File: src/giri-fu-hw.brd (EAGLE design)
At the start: 91.1 x 54.6 mm, 30 parts, among them IC1 ATMEGA168-20P, IC2 7805T, IC3 ULN2003AN, K1 G5V1, K2 G5V1, K3 G5V1, K4 G5V1, K5 G5V1, K6 G5V1, Q1 16MHz

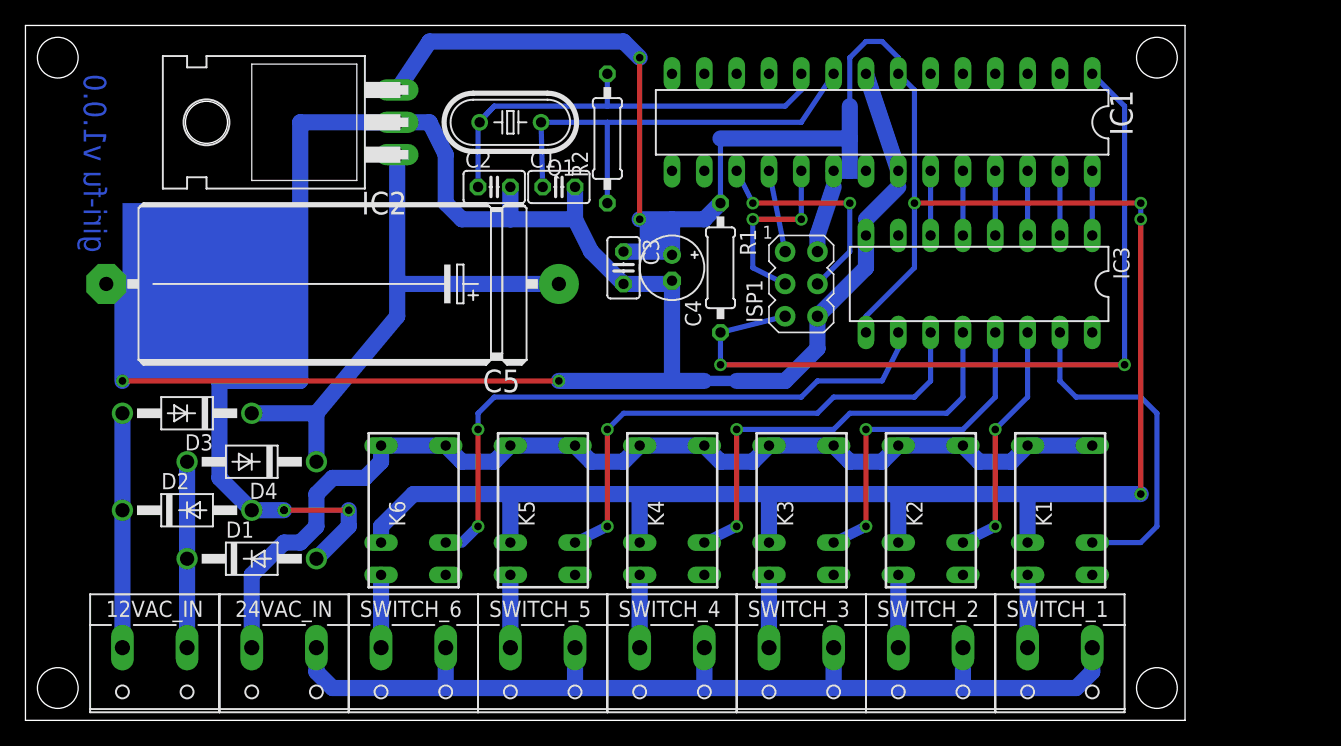
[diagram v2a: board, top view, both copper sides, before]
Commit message: Add RS485 adapter
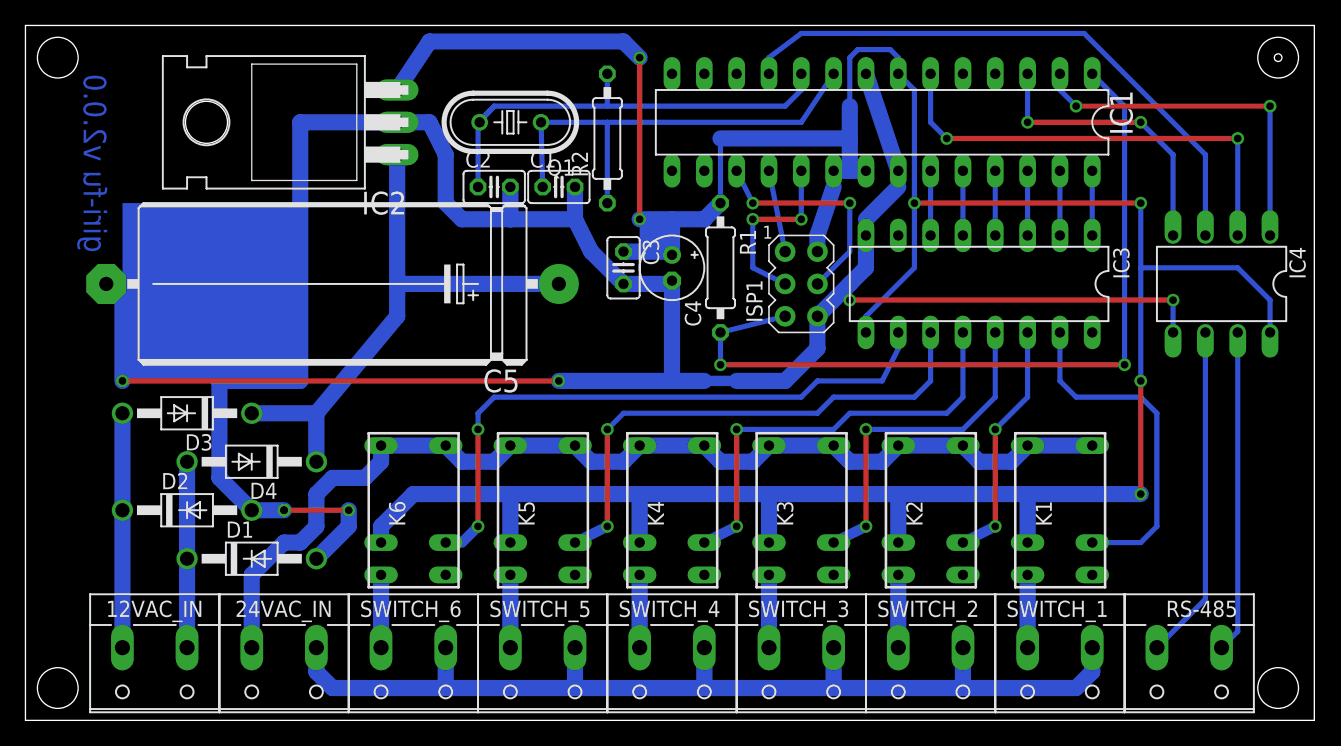
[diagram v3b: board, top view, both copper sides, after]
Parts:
- added IC4: MAX485, max485:DIL08
- added RS-485: (no value), con-wago-508:W237-132
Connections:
- new net N$24: IC4.6, RS-485.2
- new net N$25: IC4.7, RS-485.1
- new net N$26: IC1.2, IC4.1
- new net N$27: IC1.3, IC4.4
- new net N$36: IC1.6, IC4.2
- new net N$38: IC1.11, IC4.3
- net GND: now also IC4.5
- net N$8: now also IC4.8
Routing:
- net N$38: track 0.00 -> 46.5 mm
- net N$36: track 0.00 -> 36.1 mm, vias 0 -> 2
- net GND: track 201.3 -> 230.5 mm, vias 4 -> 6
- net N$26: track 0.00 -> 28.5 mm, vias 0 -> 2
- net N$24: track 0.00 -> 26.3 mm
- net N$25: track 0.00 -> 25.3 mm
- net N$27: track 0.00 -> 22.6 mm, vias 0 -> 2
- net N$8: track 231.3 -> 244.5 mm
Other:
- board size 91.1 x 54.6 mm -> 101.3 x 54.6 mm
- board text added: "giri-fu v2.0.0"
- board text removed: "giri-fu v1.0.0"
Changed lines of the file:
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@@
 <setting verticaltext="up"/>
 </settings>
-<grid distance="0.05" unitdist="inch" unit="inch" style="lines" multiple="1" display="no" altdistance="0.025" altunitdist="inch" altunit="inch"/>
+<grid distance="0.025" unitdist="inch" unit="inch" style="lines" multiple="1" display="no" altdistance="0.025" altunitdist="inch" altunit="inch"/>
 <layers>
 <layer number="1" name="Top" color="4" fill="1" visible="yes" active="yes"/>
@@
 <layer number="43" name="vRestrict" color="2" fill="10" visible="no" active="yes"/>
 <layer number="44" name="Drills" color="7" fill="1" visible="no" active="yes"/>
-<layer number="45" name="Holes" color="7" fill="1" visible="no" active="yes"/>
+<layer number="45" name="Holes" color="7" fill="1" visible="yes" active="yes"/>
 <layer number="46" name="Milling" color="3" fill="1" visible="no" active="yes"/>
 <layer number="47" name="Measures" color="7" fill="1" visible="no" active="yes"/>
@@
 <board>
 <plain>
-<wire x1="0" y1="0" x2="91.11" y2="0" width="0" layer="20"/>
-<wire x1="91.11" y1="0" x2="91.11" y2="54.6" width="0" layer="20"/>
-<wire x1="91.11" y1="54.6" x2="0" y2="54.6" width="0" layer="20"/>
+<wire x1="0" y1="0" x2="101.27" y2="0" width="0" layer="20"/>
+<wire x1="101.27" y1="0" x2="101.27" y2="54.6" width="0" layer="20"/>
+<wire x1="101.27" y1="54.6" x2="0" y2="54.6" width="0" layer="20"/>
 <wire x1="0" y1="54.6" x2="0" y2="0" width="0" layer="20"/>
-<hole x="88.9" y="2.54" drill="3.2"/>
+<hole x="98.425" y="2.54" drill="3.2"/>
 <rectangle x1="7.62" y1="26.67" x2="15.24" y2="34.29" layer="16"/>
 <hole x="2.54" y="2.54" drill="3.2"/>
 <hole x="2.54" y="52.07" drill="3.2"/>
-<hole x="88.9" y="52.07" drill="3.2"/>
-<text x="6.35" y="50.8" size="1.778" layer="16" rot="MR270">giri-fu v1.0.0</text>
+<hole x="98.425" y="52.07" drill="3.2"/>
+<text x="6.35" y="50.8" size="1.778" layer="16" rot="MR270">giri-fu v2.0.0</text>
 <text x="40.894" y="39.624" size="1.27" layer="125" ratio="10">C1</text>
 <text x="35.814" y="39.624" size="1.27" layer="125" ratio="10">C2</text>
@@
 <rectangle x1="48.26" y1="36.83" x2="50.8" y2="39.37" layer="16"/>
 <rectangle x1="7.62" y1="26.67" x2="21.59" y2="40.64" layer="16"/>
+<hole x="98.425" y="52.07" drill="0.6"/>
 </plain>
 <attributes>
@@
 <attribute name="OC_FARNELL" value="unknown" x="10.16" y="5.08" size="1.778" layer="27" rot="R180" display="off"/>
 </element>
+<element name="RS-485" library="con-wago-508" package="W237-132" value="" x="91.44" y="5.08" rot="R180">
+<attribute name="OC_FARNELL" value="unknown" x="91.44" y="5.08" size="1.778" layer="27" rot="R180" display="off"/>
+<attribute name="MPN" value="" x="91.44" y="5.08" size="1.778" layer="27" rot="R180" display="off"/>
+<attribute name="MF" value="" x="91.44" y="5.08" size="1.778" layer="27" rot="R180" display="off"/>
+<attribute name="OC_NEWARK" value="unknown" x="91.44" y="5.08" size="1.778" layer="27" rot="R180" display="off"/>
+</element>
+<element name="IC4" library="max485" package="DIL08" value="MAX485" x="93.98" y="34.29" rot="R180">
+<attribute name="MOUSER_PARTNO" value="MAX485ECPA+" x="93.98" y="34.29" size="1.778" layer="27" rot="R180" display="off"/>
+<attribute name="MANUFACTURER_PARTNO" value="MAX485ECPA+" x="93.98" y="34.29" size="1.778" layer="27" rot="R180" display="off"/>
+</element>
 </elements>
 <signals>
@@
 <wire x1="50.8" y1="26.67" x2="50.8" y2="34.544" width="1.27" layer="16"/>
 <wire x1="66.04" y1="50.8" x2="68.58" y2="43.18" width="1.27" layer="16"/>
-<wire x1="62.23" y1="31.75" x2="66.04" y2="35.56" width="1.27" layer="16"/>
+<wire x1="62.23" y1="31.75" x2="64.77" y2="34.29" width="1.27" layer="16"/>
+<wire x1="64.77" y1="34.29" x2="66.04" y2="35.56" width="1.27" layer="16"/>
 <wire x1="66.04" y1="35.56" x2="66.04" y2="38.1" width="1.27" layer="16"/>
 <wire x1="46.99" y1="34.29" x2="44.45" y2="36.83" width="1.27" layer="16"/>
@@
 <wire x1="17.78" y1="16.51" x2="15.24" y2="19.05" width="1.27" layer="16"/>
 <wire x1="15.24" y1="19.05" x2="15.24" y2="26.67" width="1.27" layer="16"/>
-<wire x1="25.4" y1="16.51" x2="25.4" y2="15.24" width="0" layer="19" extent="16-16"/>
+<contactref element="IC4" pad="5"/>
+<wire x1="90.17" y1="30.48" x2="90.17" y2="33.02" width="0.4064" layer="16"/>
+<via x="90.17" y="33.02" extent="1-16" drill="0.6" shape="square"/>
+<wire x1="90.17" y1="33.02" x2="64.77" y2="33.02" width="0.4064" layer="1"/>
+<via x="64.77" y="33.02" extent="1-16" drill="0.6" shape="square"/>
+<wire x1="64.77" y1="33.02" x2="64.77" y2="34.29" width="0.4064" layer="16"/>
 </signal>
 <signal name="N$12">
@@
 <wire x1="62.23" y1="38.1" x2="62.23" y2="36.83" width="1.27" layer="16"/>
 <wire x1="68.58" y1="50.8" x2="68.58" y2="52.07" width="0.4064" layer="16"/>
-<wire x1="68.58" y1="52.07" x2="67.31" y2="53.34" width="0.4064" layer="16"/>
-<wire x1="67.31" y1="53.34" x2="66.04" y2="53.34" width="0.4064" layer="16"/>
-<wire x1="66.04" y1="53.34" x2="64.77" y2="52.07" width="0.4064" layer="16"/>
+<wire x1="68.58" y1="52.07" x2="67.945" y2="52.705" width="0.4064" layer="16"/>
+<wire x1="67.945" y1="52.705" x2="65.405" y2="52.705" width="0.4064" layer="16"/>
+<wire x1="65.405" y1="52.705" x2="64.77" y2="52.07" width="0.4064" layer="16"/>
 <wire x1="64.77" y1="52.07" x2="64.77" y2="48.26" width="0.4064" layer="16"/>
 <wire x1="64.77" y1="48.26" x2="64.77" y2="45.72" width="1.27" layer="16"/>
@@
 <wire x1="69.85" y1="40.64" x2="87.63" y2="40.64" width="0.4064" layer="1"/>
 <via x="87.63" y="40.64" extent="1-16" drill="0.6" shape="square"/>
-<wire x1="87.63" y1="40.64" x2="87.63" y2="39.37" width="0.4064" layer="16"/>
-<via x="87.63" y="39.37" extent="1-16" drill="0.6" shape="square"/>
-<wire x1="87.63" y1="39.37" x2="87.63" y2="17.78" width="0.4064" layer="1"/>
+<wire x1="87.63" y1="40.64" x2="87.63" y2="35.56" width="0.4064" layer="16"/>
+<via x="87.63" y="26.67" extent="1-16" drill="0.6" shape="square"/>
+<wire x1="87.63" y1="35.56" x2="87.63" y2="26.67" width="0.4064" layer="16"/>
+<wire x1="87.63" y1="26.67" x2="87.63" y2="17.78" width="0.4064" layer="1"/>
 <via x="87.63" y="17.78" extent="1-16" drill="0.6" shape="square"/>
 <wire x1="87.63" y1="17.78" x2="78.74" y2="17.78" width="1.27" layer="16"/>
+<contactref element="IC4" pad="8"/>
+<wire x1="97.79" y1="30.48" x2="97.79" y2="33.02" width="0.4064" layer="16"/>
+<wire x1="97.79" y1="33.02" x2="95.25" y2="35.56" width="0.4064" layer="16"/>
+<wire x1="95.25" y1="35.56" x2="87.63" y2="35.56" width="0.4064" layer="16"/>
+</signal>
+<signal name="N$26">
+<contactref element="IC1" pad="2"/>
+<contactref element="IC4" pad="1"/>
+<wire x1="81.28" y1="50.8" x2="81.28" y2="49.53" width="0.4064" layer="16"/>
+<wire x1="81.28" y1="49.53" x2="82.55" y2="48.26" width="0.4064" layer="16"/>
+<via x="82.55" y="48.26" extent="1-16" drill="0.6" shape="square"/>
+<wire x1="82.55" y1="48.26" x2="97.79" y2="48.26" width="0.4064" layer="1"/>
+<via x="97.79" y="48.26" extent="1-16" drill="0.6" shape="square"/>
+<wire x1="97.79" y1="48.26" x2="97.79" y2="38.1" width="0.4064" layer="16"/>
+</signal>
+<signal name="N$27">
+<contactref element="IC1" pad="3"/>
+<contactref element="IC4" pad="4"/>
+<wire x1="78.74" y1="50.8" x2="78.74" y2="46.99" width="0.4064" layer="16"/>
+<via x="78.74" y="46.99" extent="1-16" drill="0.6" shape="square"/>
+<wire x1="78.74" y1="46.99" x2="87.63" y2="46.99" width="0.4064" layer="1"/>
+<via x="87.63" y="46.99" extent="1-16" drill="0.6" shape="square"/>
+<wire x1="87.63" y1="46.99" x2="90.17" y2="44.45" width="0.4064" layer="16"/>
+<wire x1="90.17" y1="44.45" x2="90.17" y2="38.1" width="0.4064" layer="16"/>
+</signal>
+<signal name="N$36">
+<contactref element="IC1" pad="6"/>
+<contactref element="IC4" pad="2"/>
+<wire x1="71.12" y1="50.8" x2="71.12" y2="46.99" width="0.4064" layer="16"/>
+<wire x1="71.12" y1="46.99" x2="72.39" y2="45.72" width="0.4064" layer="16"/>
+<via x="72.39" y="45.72" extent="1-16" drill="0.6" shape="square"/>
+<wire x1="72.39" y1="45.72" x2="95.25" y2="45.72" width="0.4064" layer="1"/>
+<via x="95.25" y="45.72" extent="1-16" drill="0.6" shape="square"/>
+<wire x1="95.25" y1="45.72" x2="95.25" y2="38.1" width="0.4064" layer="16"/>
+</signal>
+<signal name="N$38">
+<contactref element="IC1" pad="11"/>
+<contactref element="IC4" pad="3"/>
+<wire x1="58.42" y1="50.8" x2="58.42" y2="52.07" width="0.4064" layer="16"/>
+<wire x1="58.42" y1="52.07" x2="60.96" y2="53.975" width="0.4064" layer="16"/>
+<wire x1="60.96" y1="53.975" x2="83.185" y2="53.975" width="0.4064" layer="16"/>
+<wire x1="83.185" y1="53.975" x2="92.71" y2="44.45" width="0.4064" layer="16"/>
+<wire x1="92.71" y1="44.45" x2="92.71" y2="38.1" width="0.4064" layer="16"/>
+</signal>
+<signal name="N$24">
+<contactref element="IC4" pad="6"/>
+<contactref element="RS-485" pad="2"/>
+<wire x1="92.71" y1="30.48" x2="92.71" y2="9.525" width="0.4064" layer="16"/>
+<wire x1="92.71" y1="9.525" x2="88.9" y2="5.715" width="0.4064" layer="16"/>
+</signal>
+<signal name="N$25">
+<contactref element="IC4" pad="7"/>
+<contactref element="RS-485" pad="1"/>
+<wire x1="95.25" y1="30.48" x2="95.25" y2="6.985" width="0.4064" layer="16"/>
+<wire x1="95.25" y1="6.985" x2="93.98" y2="5.715" width="0.4064" layer="16"/>
 </signal>
 </signals>
